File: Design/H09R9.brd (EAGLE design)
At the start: 34.6 x 30 mm, 24 parts, among them P1 HEXABIT_17.32, U1 STM32F091CBU6, U2 TSD305-1C55, X1 XTALL_CSTCE8M00G52

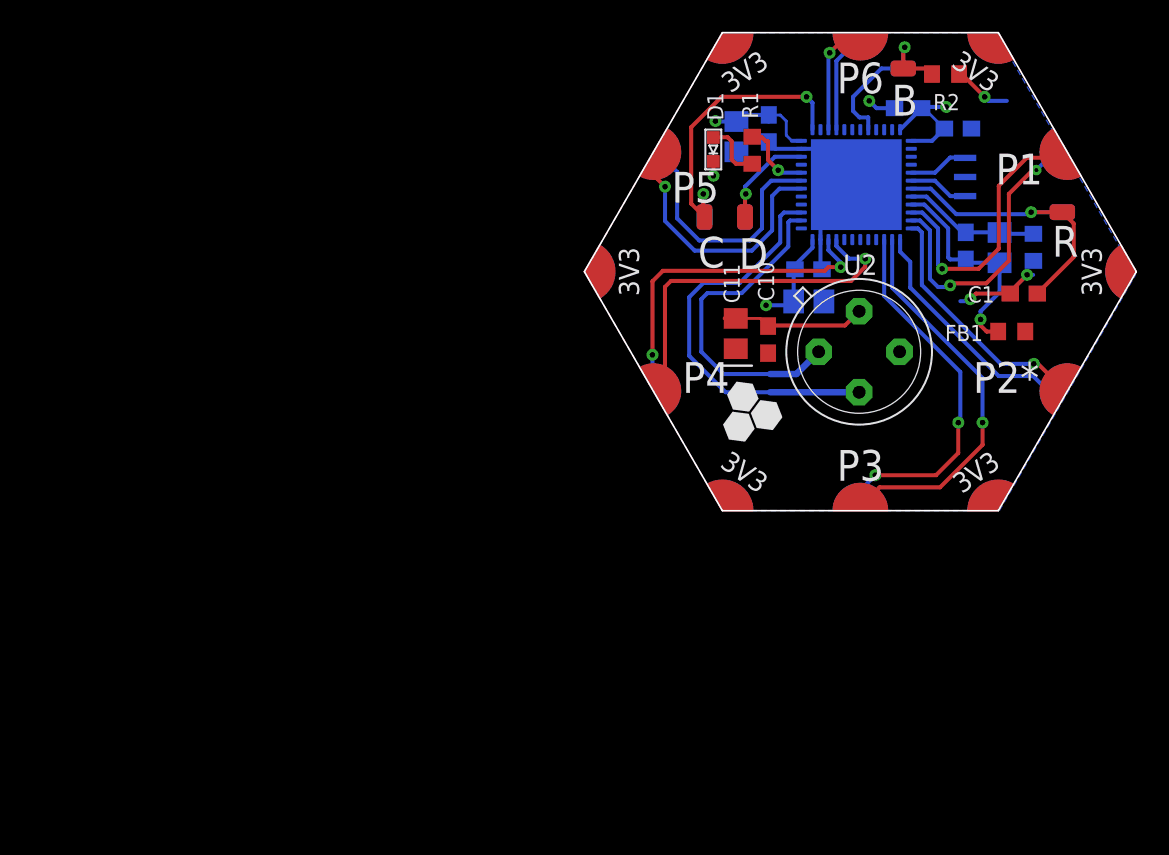
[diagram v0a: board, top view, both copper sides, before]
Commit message: - The reviewed version is complete. - The upgraded version features the STM32G0B1CEU6N MCU. - Pull-up resistors have been added to the I2C Bus.
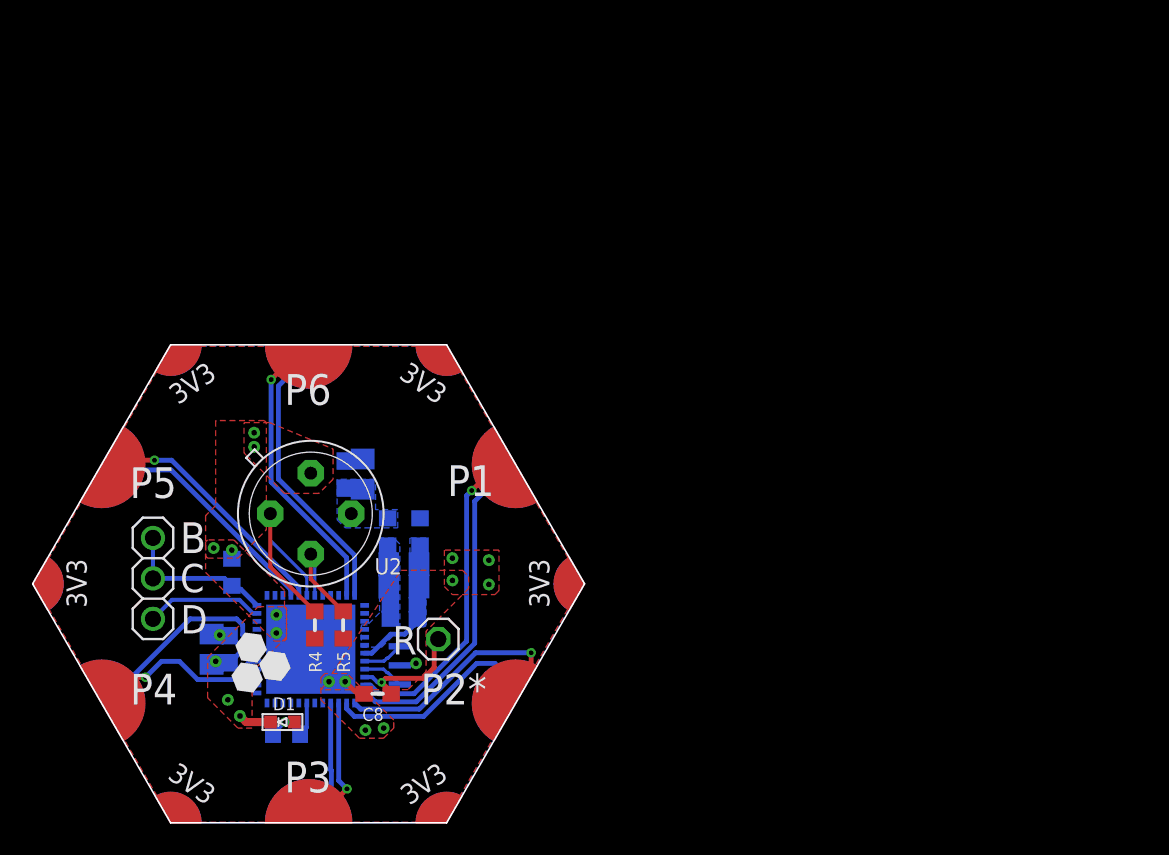
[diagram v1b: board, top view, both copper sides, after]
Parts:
- removed B, C, D: PAD1, Hexabitz:PAD1
- removed C5: 10nF, Hexabitz:C-0603
- removed C9: 100nF, Hexabitz:C-0603
- added JP2: (no value), pinhead:1X03
- added R4, R5: 10K, HEXABITZ_RCLS:R-0603
- C1, C10, C6, C7, C8: device Hexabitz:C-0603 -> HEXABITZ_RCLS:C-0603
- C11, C3, C4: device Hexabitz:C-0805-POL -> HEXABITZ_RCLS:C-0805-POL
- C2: value 1.00uF -> 1uF; device Hexabitz:C-0805-POL -> HEXABITZ_RCLS:C-0805-POL
- D1: value VLMS1300-GS08 -> RED; device Hexabitz:VLMS1300-GS08 -> HEXABITZ_USER_INTERFACE_PARTS:VLMS1300-GS08
- FB1: device Hexabitz:FB-TDK_MMZ1608Y300B -> HEXABITZ_RCLS:FB-TDK_MMZ1608Y300B
- P1: device Hexabitz:HEXABIT_17.32 -> hexabitz_connectors:HEXABIT_17.32
- R: value PAD1 -> R; device Hexabitz:PAD1 -> HEXABITZ_USER_INTERFACE_PARTS:1X01
- R1: value 270.0R -> 270R; device Hexabitz:R-0603 -> HEXABITZ_RCLS:R-0603
- R2: value 10.0K -> 10K; device Hexabitz:R-0603 -> HEXABITZ_RCLS:R-0603
- R3: device Hexabitz:R-0603 -> HEXABITZ_RCLS:R-0603
- U1: value STM32F091CBU6 -> STM32G0B1CEU6N; device Hexabitz:STM32F091CBU6 -> HEXABITZ_ICs:HEXABITZ_ICS_QFN_B1CEU6_STM-L
- X1: device Hexabitz:XTALL_CSTCE8M00G52 -> HEXABITZ_RCLS:XTALL_CSTCE8M00G52
- moved R2 54.6 mm to (-4.83, 15.7), flipped to the bottom, turned to 270 degrees
- moved R 47.5 mm to (8.13, 11.6), turned to 0 degrees
- moved C7 47.0 mm to (-4.95, 10.9)
- moved X1 46.9 mm to (5.71, 9.91), turned to 180 degrees
- moved R1 46.9 mm to (-1.40, 5.59), flipped to the bottom, turned to 0 degrees
- moved C4 46.0 mm to (-6.10, 10.9)
- moved C6 45.0 mm to (5.97, 12.8), turned to 180 degrees
- moved D1 45.0 mm to (-1.65, 6.35), turned to 270 degrees
- moved U1 45.0 mm to (0.13, 10.9), turned to 0 degrees
- moved C1 43.5 mm to (5.97, 13.7), flipped to the bottom
- moved C2 43.0 mm to (5.97, 14.9), turned to 180 degrees
- moved R3 42.4 mm to (6.99, 18.3), turned to 270 degrees
- moved FB1 41.1 mm to (4.95, 18.3), flipped to the bottom, turned to 90 degrees
- moved P1 39.8 mm to (-0.01, 15.0)
- moved C8 38.0 mm to (4.32, 8.13), flipped to the top
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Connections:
- removed net B1: B.P$1, B.P$2, R2.2, U1.P$44
- removed net IMU_INT2: U1.P$16
- removed net MAG_INT: U1.P$17
- removed net R1: C1.1, R.P$1, R.P$2, U1.P$7
- removed net SWCLK: C.P$1, C.P$2, U1.P$37
- removed net SWD: D.P$1, D.P$2, U1.P$34
- removed net XL_INT1: U1.P$19
- removed net XL_INT2: U1.P$18
- new net CLK: JP2.1, JP2.2, R2.2, U1.36
- new net DATA: JP2.3, U1.35
- new net N$1: R1.1, U1.19
- net GND: now also U1.30, U1.49; no longer C1.2, C3.2, C6.2, C9.2, U1.EP, U1.P$23, U1.P$35, U1.P$45, U1.P$46, U1.P$47
- net I2C2_SCL: now also R4.1, U1.42; no longer U1.P$26
- net I2C2_SDA: now also R5.1, U1.43; no longer U1.P$27
- net N$3: now also D1.A; no longer U1.P$32
- net N$4: now also C8.1, R.1, U1.10; no longer D1.A, R1.1
- net N$5: now also U1.9; no longer U1.P$5
- net N$6: now also U1.8; no longer U1.P$6
- net USART1_RX: now also P1.PAD_PD4, U1.32; no longer P1.PAD_PD5, U1.P$31
- net USART1_TX: now also P1.PAD_PU4, U1.29; no longer P1.PAD_PU5, U1.P$30
- net USART2_RX: now also U1.14; no longer U1.P$13
- net USART2_TX: now also U1.13; no longer U1.P$12
- net USART3_RX: now also P1.PAD_PD6, U1.48; no longer P1.PAD_PD4, U1.P$22
- net USART3_TX: now also P1.PAD_PU6, U1.47; no longer P1.PAD_PU4, U1.P$21
- net USART4_RX: now also U1.12; no longer U1.P$11
- net USART4_TX: now also U1.11; no longer U1.P$10
- net USART5_RX: now also P1.PAD_PD5, U1.40; no longer P1.PAD_PD6, U1.P$40
- net USART5_TX: now also P1.PAD_PU5, U1.41; no longer P1.PAD_PU6, U1.P$39
- net USART6_RX: now also U1.16; no longer U1.P$15
- net USART6_TX: now also U1.15; no longer U1.P$14
- net VDD: now also R4.2, R5.2, U1.31; no longer C3.1, C6.1, C8.1, C9.1, U1.P$1, U1.P$24, U1.P$36, U1.P$48
- net VDDA: now also C1.1, C3.1, C6.1, U1.4, U1.5, U1.6; no longer C5.1, U1.P$9
- net VSSA: now also C1.2, C3.2, C6.2, U1.7; no longer C5.2, U1.P$8
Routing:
- net GND: track 36.3 -> 6.71 mm, vias 5 -> 18
- net SWCLK: track 19.2 -> 0.00 mm, vias 2 -> 0
- net R1: track 18.5 -> 0.00 mm, vias 1 -> 0
- net I2C2_SDA: track 25.5 -> 7.13 mm
- net VDD: track 21.6 -> 3.78 mm, vias 3 -> 1
- net USART6_RX: track 23.2 -> 7.44 mm, vias 2 -> 0
- net USART6_TX: track 24.3 -> 8.61 mm
- net VDDA: track 13.8 -> 0.00 mm, vias 1 -> 0
- net B1: track 11.5 -> 0.00 mm, vias 1 -> 0
- net CLK: track 0.00 -> 9.77 mm
- net USART5_TX: track 7.17 -> 15.8 mm
- net USART5_RX: track 6.27 -> 14.7 mm
- net SWD: track 7.86 -> 0.00 mm, vias 1 -> 0
- net I2C2_SCL: track 21.0 -> 13.4 mm
- net DATA: track 0.00 -> 7.37 mm
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- added copper zone on layer 1, net GND
- added copper zone on layer 16, net VDD
- added copper zone on layer 16, net VDDA
- added copper zone on layer 16, net VSSA
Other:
- board text added: "H09R91"
- board text removed: "H09R90"
- board text removed: "R"
